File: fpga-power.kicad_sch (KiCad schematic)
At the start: 100 parts, among them U4 XC7K160T-FFG676

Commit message: Finish schematic cleanup
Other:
- note added: "FPGA Power rails"
- note removed: "POWER RAILS"
- moved on the sheet: C100, C101, C102, C103, C104, C105, C106, C107, C108, C11, C12, C13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

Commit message: Clean schematic DRC
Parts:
- C12, C25, C38: Dielectric template_dielectric -> (none)

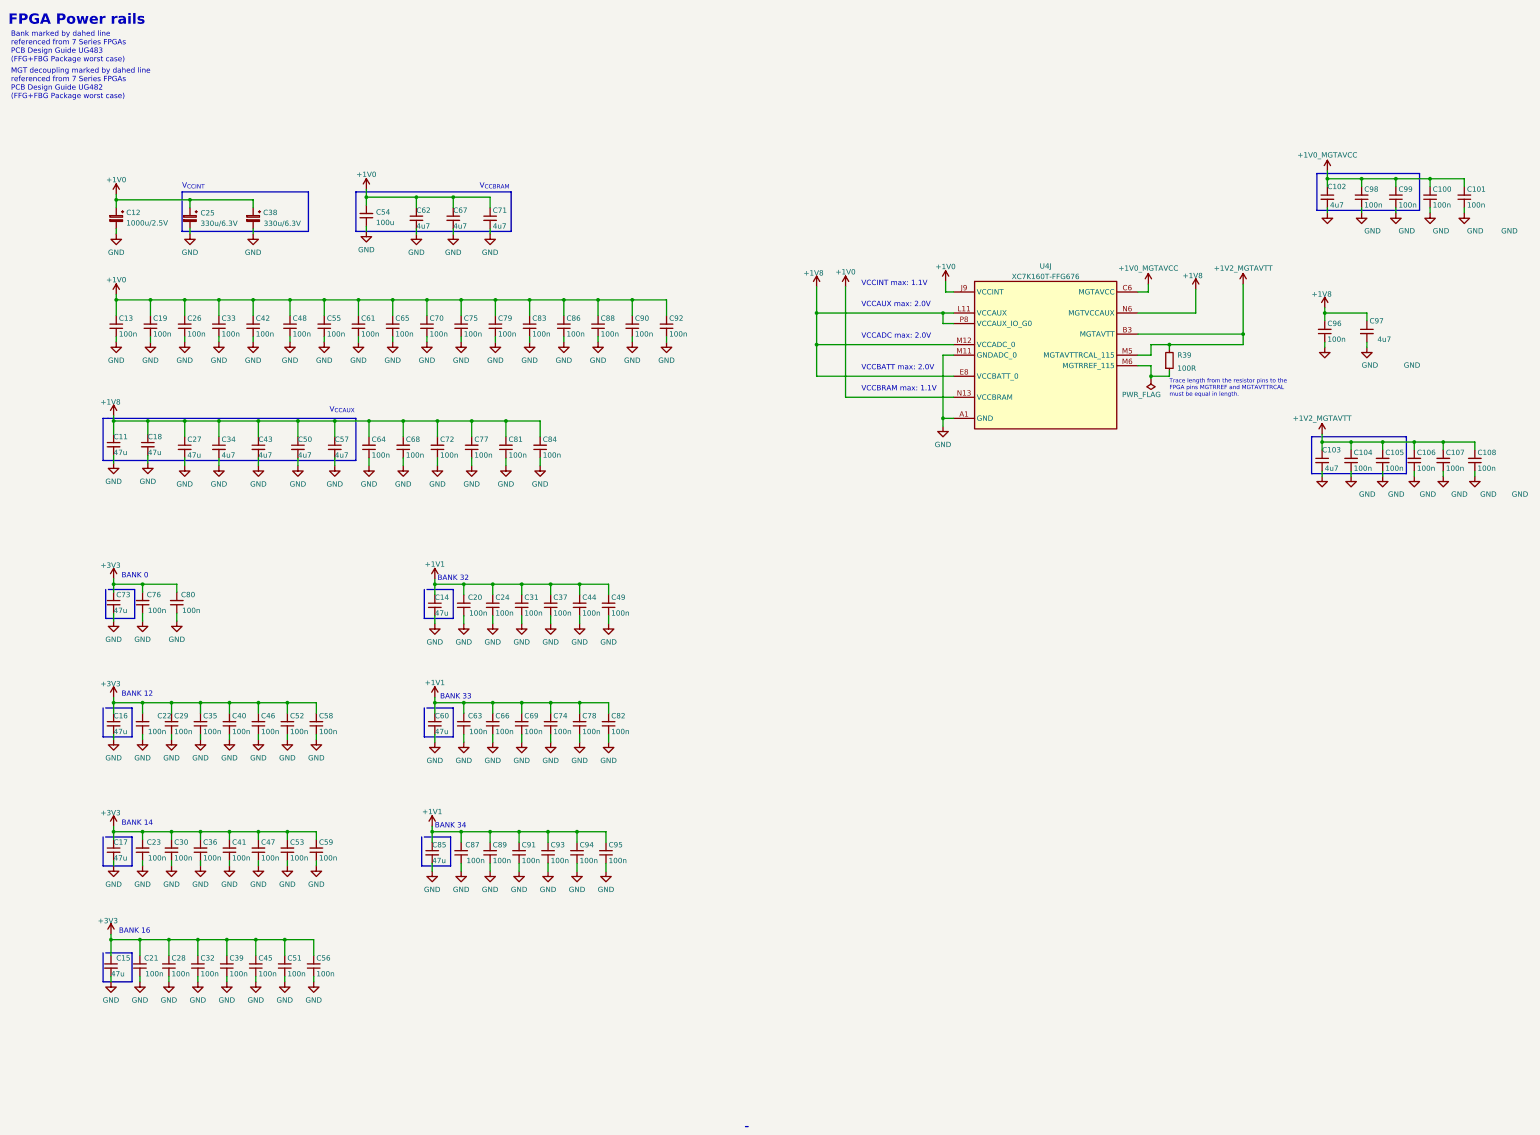
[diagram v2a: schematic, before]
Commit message: Add updated components to local library
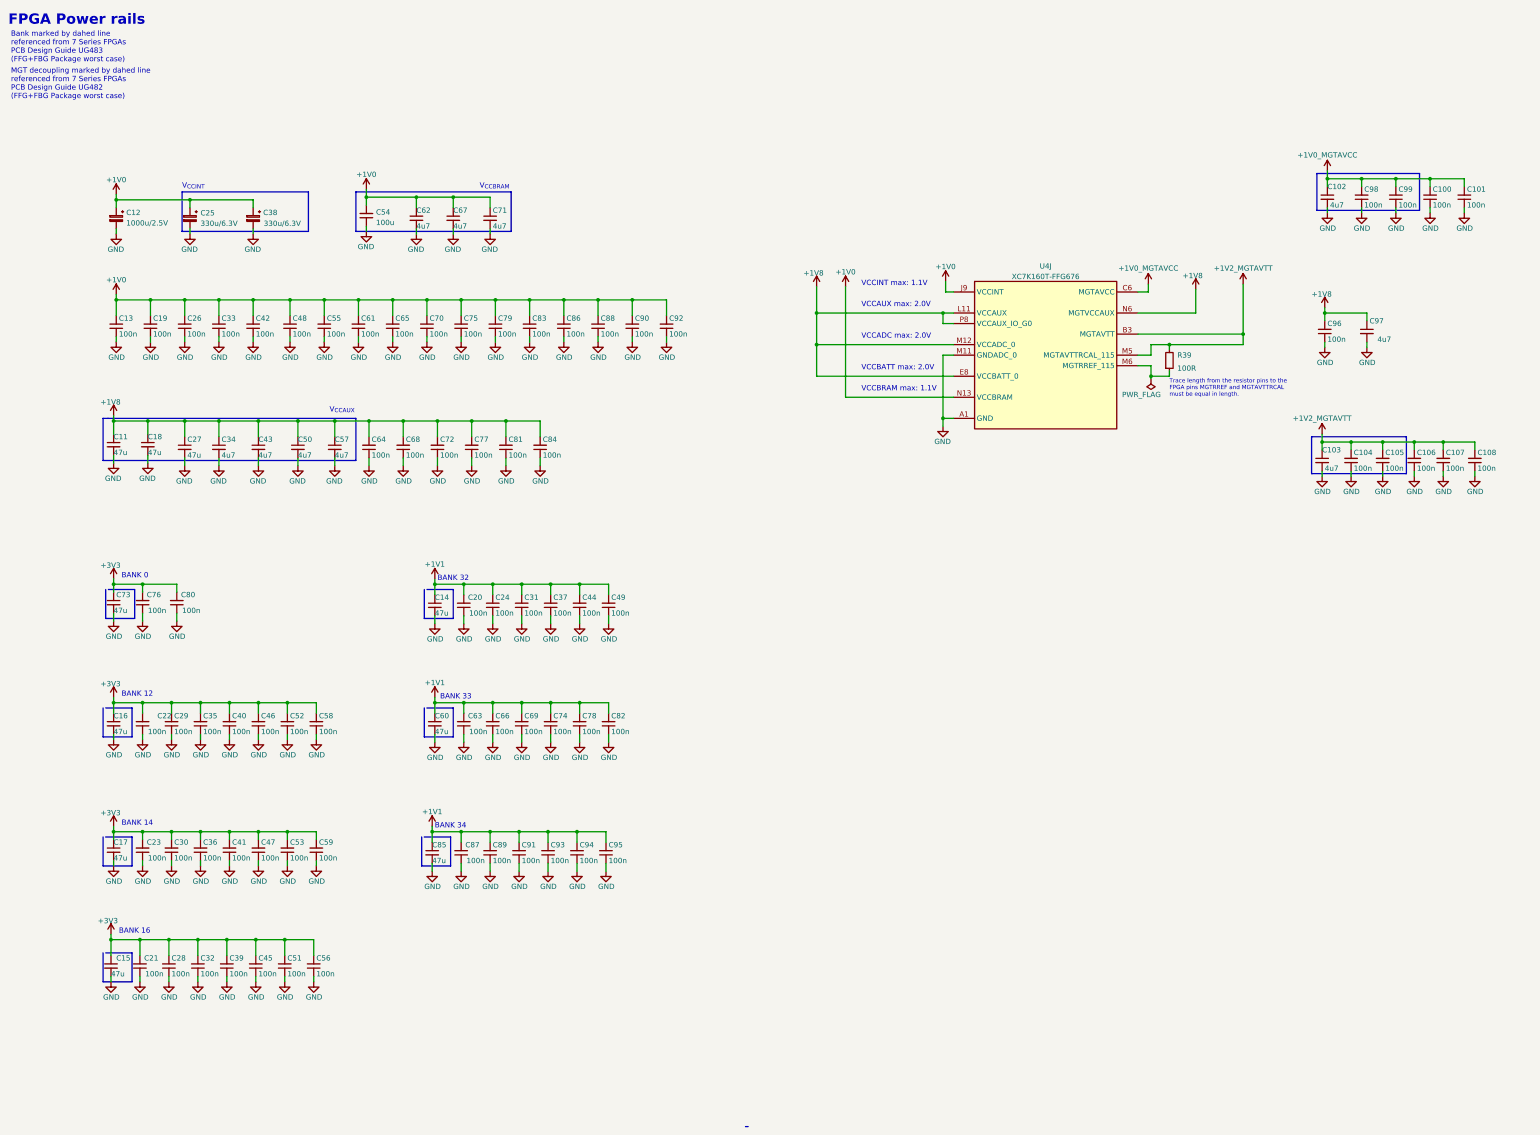
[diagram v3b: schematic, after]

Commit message: [#57478] ohp release
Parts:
- C100, C101, C104, C105, C106, C107, C108, C13, C19, C20, C21, C22, C23, C24, C26, C28, C29, C30, C31, C32, C33, C35, C36, C37, C39, C40, C41, C42, C44, C45, C46, C47, C48, C49, C51, C52, C53, C55, C56, C58, C59, C61, C63, C64, C65, C66, C68, C69, C70, C72, C74, C75, C76, C77, C78, C79, C80, C81, C82, C83, C84, C86, C87, C88, C89, C90, C91, C92, C93, C94, C95, C96, C98, C99: footprint sodimm-ddr5-tester-footprints:C_0402_1005Metric_EIA -> antmicro-footprints:C_0402_1005Metric; symbol sodimm-ddr5-tester:C_100n_0402 -> antmicroCapacitors0402:C_100n_0402
- C102, C103, C34, C43, C50, C57, C62, C67, C71, C97: footprint sodimm-ddr5-tester-footprints:C_0402_1005Metric_EIA -> antmicro-footprints:C_0402_1005Metric; symbol sodimm-ddr5-tester:C_4u7_0402 -> antmicroCapacitors0402:C_4u7_0402
- C11, C14, C15, C16, C17, C18, C27, C60, C73, C85: footprint sodimm-ddr5-tester-footprints:C_0603_1608Metric -> antmicro-footprints:C_0603_1608Metric; symbol sodimm-ddr5-tester:C_47u_0603 -> antmicroCapacitors0603:C_47u_0603
- C12: footprint sodimm-ddr5-tester-footprints:C_Pol_EIA-D -> antmicro-footprints:C_Pol_EIA-D; symbol sodimm-ddr5-tester:C_Pol_1m_2.5V_KEMET-T520-D -> antmicroCapacitorspol:C_Pol_1m_2.5V_KEMET-T520-D
- C25, C38: footprint sodimm-ddr5-tester-footprints:C_Pol_EIA-B -> antmicro-footprints:C_Pol_EIA-B; symbol sodimm-ddr5-tester:C_Pol_330u_6.3V_KEMET-T520-B -> antmicroCapacitorspol:C_Pol_330u_6.3V_KEMET-T520-B
- C54: footprint sodimm-ddr5-tester-footprints:C_0805_2012Metric -> antmicro-footprints:C_0805_2012Metric; symbol sodimm-ddr5-tester:C_100u_0805 -> antmicroCapacitorsmisc:C_100u_0805
- R39: footprint sodimm-ddr5-tester-footprints:R_0402_1005Metric_EIA -> antmicro-footprints:R_0402_1005Metric; symbol sodimm-ddr5-tester:R_100R_0402 -> antmicroResistors0402:R_100R_0402
- U4: footprint sodimm-ddr5-tester-footprints:BGA-676_27x27mm_Layout26x26_P1X1mm -> antmicro-footprints:BGA-676_27x27mm_Layout26x26_P1x1mm_FFG676; symbol sodimm-ddr5-tester:XC7K160T-FFG676 -> antmicroFPGAChips:XC7K160T-FFG676

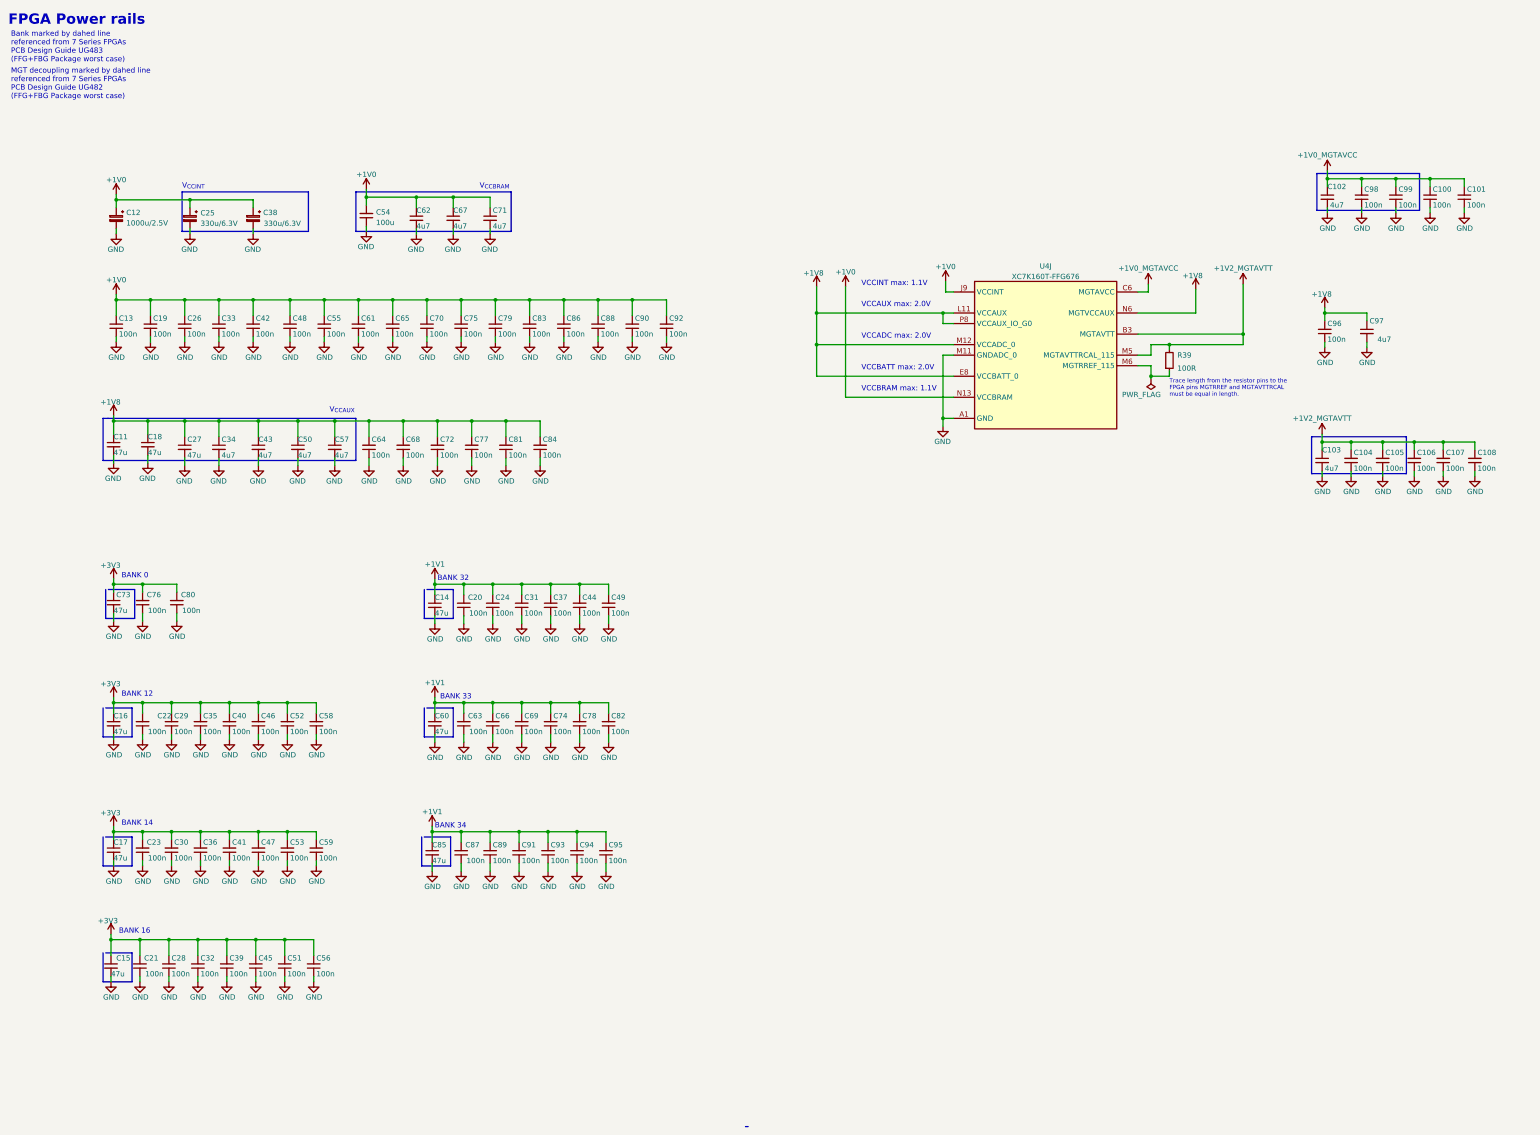
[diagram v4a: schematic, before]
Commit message: [#58418] Update obsolete MPNs. Replace fuses. Remap PWR_EN and PWR_GOOD. Add UART logic level conventers. Bump revision to 1.2.0
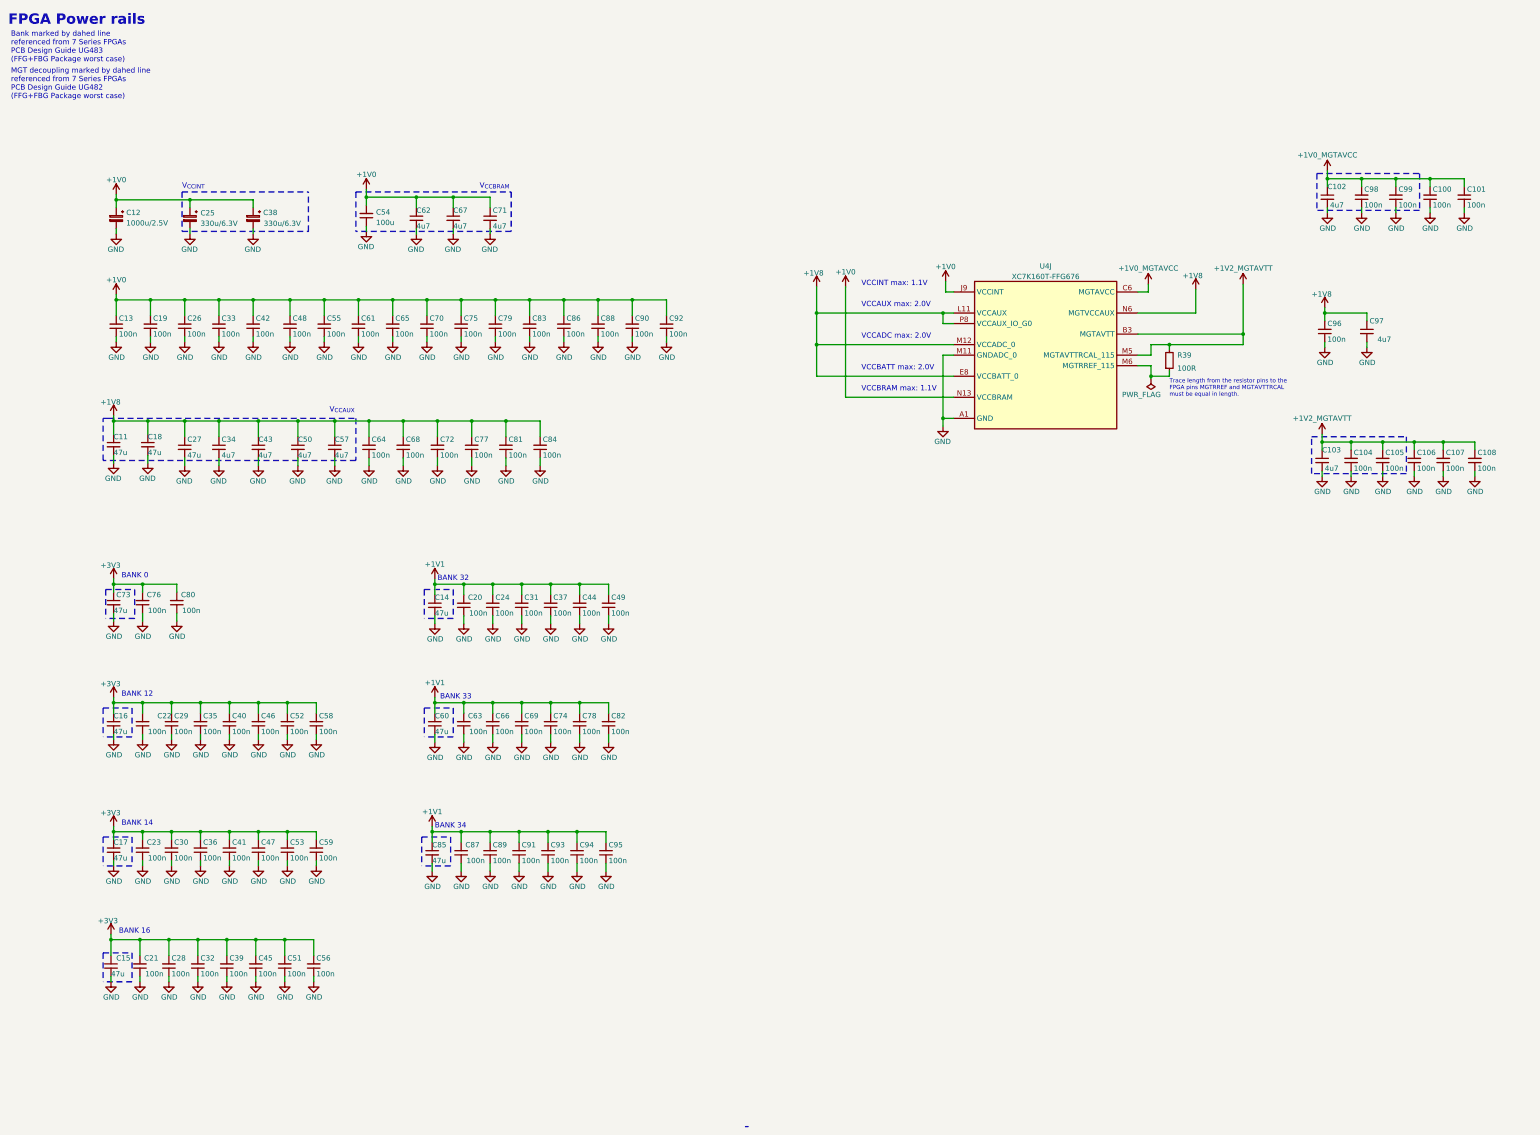
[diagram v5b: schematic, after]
